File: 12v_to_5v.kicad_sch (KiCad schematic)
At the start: 6 parts, among them U5 ADP1108AR-5

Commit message: Woops
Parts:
- renumbered C11 to C10, C10 to C11, D2 to D3, R2 to R4, U5 to U4
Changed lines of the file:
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@@
 		(instances
 			(project "cabinet_light"
-				(path "/8f50e6d6-3696-4153-9907-ddc1ca4e5be3/20de0641-49d0-48c6-ac6e-db96bd849d07"
+				(path "/8f50e6d6-3696-4153-9907-ddc1ca4e5be3/8515131e-704f-44f3-9e5f-b6c790cb260b"
 					(reference "L2")
 					(unit 1)
@@
 		(on_board yes)
 		(dnp no)
-		(property "Reference" "C11"
+		(property "Reference" "C10"
 			(at 114.935 63.5 0)
 			(effects
@@
 		(instances
 			(project "cabinet_light"
-				(path "/8f50e6d6-3696-4153-9907-ddc1ca4e5be3/20de0641-49d0-48c6-ac6e-db96bd849d07"
-					(reference "C11")
+				(path "/8f50e6d6-3696-4153-9907-ddc1ca4e5be3/8515131e-704f-44f3-9e5f-b6c790cb260b"
+					(reference "C10")
 					(unit 1)
 				)
@@
 		(dnp no)
 		(fields_autoplaced yes)
-		(property "Reference" "#PWR029"
+		(property "Reference" "#PWR037"
 			(at 135.89 103.505 0)
 			(effects
@@
 		(instances
 			(project "cabinet_light"
-				(path "/8f50e6d6-3696-4153-9907-ddc1ca4e5be3/20de0641-49d0-48c6-ac6e-db96bd849d07"
-					(reference "#PWR029")
+				(path "/8f50e6d6-3696-4153-9907-ddc1ca4e5be3/8515131e-704f-44f3-9e5f-b6c790cb260b"
+					(reference "#PWR037")
 					(unit 1)
 				)
@@
 		(dnp no)
 		(fields_autoplaced yes)
-		(property "Reference" "#PWR016"
+		(property "Reference" "#PWR035"
 			(at 119.38 75.565 0)
 			(effects
@@
 		(instances
 			(project "cabinet_light"
-				(path "/8f50e6d6-3696-4153-9907-ddc1ca4e5be3/20de0641-49d0-48c6-ac6e-db96bd849d07"
-					(reference "#PWR016")
+				(path "/8f50e6d6-3696-4153-9907-ddc1ca4e5be3/8515131e-704f-44f3-9e5f-b6c790cb260b"
+					(reference "#PWR035")
 					(unit 1)
 				)
@@
 		(dnp no)
 		(fields_autoplaced yes)
-		(property "Reference" "#PWR0101"
+		(property "Reference" "#PWR038"
 			(at 154.305 103.505 0)
 			(effects
@@
 		(instances
 			(project "cabinet_light"
-				(path "/8f50e6d6-3696-4153-9907-ddc1ca4e5be3/20de0641-49d0-48c6-ac6e-db96bd849d07"
-					(reference "#PWR0101")
+				(path "/8f50e6d6-3696-4153-9907-ddc1ca4e5be3/8515131e-704f-44f3-9e5f-b6c790cb260b"
+					(reference "#PWR038")
 					(unit 1)
 				)
@@
 		(dnp no)
 		(fields_autoplaced yes)
-		(property "Reference" "C10"
+		(property "Reference" "C11"
 			(at 157.48 92.075 0)
 			(effects
@@
 		(instances
 			(project "cabinet_light"
-				(path "/8f50e6d6-3696-4153-9907-ddc1ca4e5be3/20de0641-49d0-48c6-ac6e-db96bd849d07"
-					(reference "C10")
+				(path "/8f50e6d6-3696-4153-9907-ddc1ca4e5be3/8515131e-704f-44f3-9e5f-b6c790cb260b"
+					(reference "C11")
 					(unit 1)
 				)
@@
 		(dnp no)
 		(fields_autoplaced yes)
-		(property "Reference" "U5"
+		(property "Reference" "U4"
 			(at 119.38 75.7271 0)
 			(effects
@@
 		(instances
 			(project "cabinet_light"
-				(path "/8f50e6d6-3696-4153-9907-ddc1ca4e5be3/20de0641-49d0-48c6-ac6e-db96bd849d07"
-					(reference "U5")
+				(path "/8f50e6d6-3696-4153-9907-ddc1ca4e5be3/8515131e-704f-44f3-9e5f-b6c790cb260b"
+					(reference "U4")
 					(unit 1)
 				)
@@
 		(dnp no)
 		(fields_autoplaced yes)
-		(property "Reference" "D2"
+		(property "Reference" "D3"
 			(at 138.43 91.7575 90)
 			(effects
@@
 		(instances
 			(project "cabinet_light"
-				(path "/8f50e6d6-3696-4153-9907-ddc1ca4e5be3/20de0641-49d0-48c6-ac6e-db96bd849d07"
-					(reference "D2")
+				(path "/8f50e6d6-3696-4153-9907-ddc1ca4e5be3/8515131e-704f-44f3-9e5f-b6c790cb260b"
+					(reference "D3")
 					(unit 1)
 				)
@@
 		(dnp no)
 		(fields_autoplaced yes)
-		(property "Reference" "#PWR020"
+		(property "Reference" "#PWR036"
 			(at 130.81 95.885 0)
 			(effects
@@
 		(instances
 			(project "cabinet_light"
-				(path "/8f50e6d6-3696-4153-9907-ddc1ca4e5be3/20de0641-49d0-48c6-ac6e-db96bd849d07"
-					(reference "#PWR020")
+				(path "/8f50e6d6-3696-4153-9907-ddc1ca4e5be3/8515131e-704f-44f3-9e5f-b6c790cb260b"
+					(reference "#PWR036")
 					(unit 1)
 				)
@@
 		(on_board yes)
 		(dnp no)
-		(property "Reference" "R2"
+		(property "Reference" "R4"
 			(at 127 63.5 0)
 			(effects
@@
 		(instances
 			(project "cabinet_light"
-				(path "/8f50e6d6-3696-4153-9907-ddc1ca4e5be3/20de0641-49d0-48c6-ac6e-db96bd849d07"
-					(reference "R2")
-					(unit 1)
-				)
+				(path "/8f50e6d6-3696-4153-9907-ddc1ca4e5be3/8515131e-704f-44f3-9e5f-b6c790cb260b"
+					(reference "R4")
+					(unit 1)
+				)

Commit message: Fix PCB
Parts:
- C10: footprint Capacitor_SMD:C_1206_3216Metric -> Capacitor_SMD:C_0603_1608Metric
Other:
- moved on the sheet: C10, C11, D3, L2, R4, U4

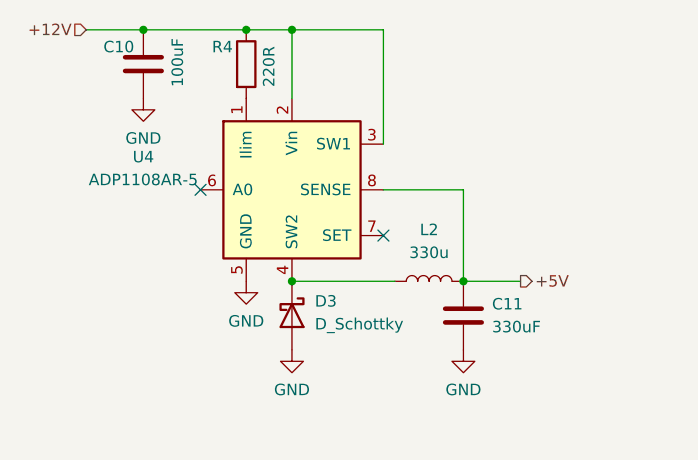
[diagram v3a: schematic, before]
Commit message: Replace power regulators; Pick all JLC components
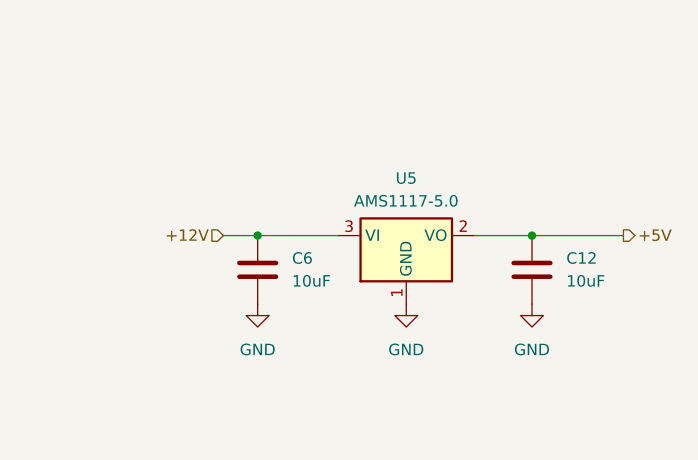
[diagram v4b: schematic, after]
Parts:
- removed C10: 100uF, Capacitor_SMD:C_0603_1608Metric, symbol Device:C
- removed C11: 330uF, Capacitor_SMD:C_0603_1608Metric, symbol Device:C
- removed D3: D_Schottky, Diode_SMD:D_0402_1005Metric, symbol Device:D_Schottky
- removed L2: 330u, Inductor_SMD:L_0603_1608Metric, symbol Device:L
- removed R4: 220R, Resistor_SMD:R_0603_1608Metric, symbol Device:R
- removed U4: ADP1108AR-5, Package_SO:SOIC-8_3.9x4.9mm_P1.27mm, symbol Regulator_Switching:ADP1108AR-5
- added C12, C6: 10uF, Capacitor_SMD:C_0805_2012Metric, symbol Device:C
- added U5: AMS1117-5.0, Package_TO_SOT_SMD:SOT-223-3_TabPin2, symbol Regulator_Linear:AMS1117-5.0
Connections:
- net +12V: now also C6.2, U5.3 (VI)
- net +5V: now also C12.2, U5.2 (VO)
- net GND: now also C12.1, C6.1, U5.1 (GND)
- no-connect marks 2 -> 0
